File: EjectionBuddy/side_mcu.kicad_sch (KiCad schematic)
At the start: 2 parts, among them U6 STM32G031K8Ux

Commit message: Finished! QR and instruction pending
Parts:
- added C15: 10u, Capacitor_SMD:C_0603_1608Metric, symbol Device:C
- added C16, C17: 0.1u, Capacitor_SMD:C_0603_1608Metric, symbol Device:C
- added R21: 1k, Resistor_SMD:R_0603_1608Metric, symbol Device:R
- added SW1: SW_Push, Button_Switch_SMD:SW_SPST_PTS810, symbol Switch:SW_Push
- D11: footprint (none) -> Diode_SMD:D_SOD-523
- renumbered U6 to U7
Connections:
- net TX: now reaches U7.22 (PA9/PA11)
- net RX: now reaches U7.23 (PA10/PA12)
- net DIO: now reaches U7.24 (PA13)
- net CLK: now reaches U7.25 (PA14)
- net at U7.31 (PB7): now also D11.2 (A)
- net at U7.32 (PB8): now also R21.1
- net GND: now reaches U7.33 (VSS), U7.5 (VSS)
- net GND: now also C15.2, C16.2, C17.2, SW1.1
- net +3.3S: now reaches U7.4 (VDD)
- net +3.3S: now also C15.1, C16.1
- net RST: now reaches U7.6 (PF2)
- net RST: now also C17.1, SW1.2
- new net ONEWIRE: R21.2
- no-connect marks 0 -> 21
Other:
- note added: "PA14 is BOOT0"
- note added: "Protection from external pulling"
- note added: "Pull high to cut"
- moved on the sheet: U7

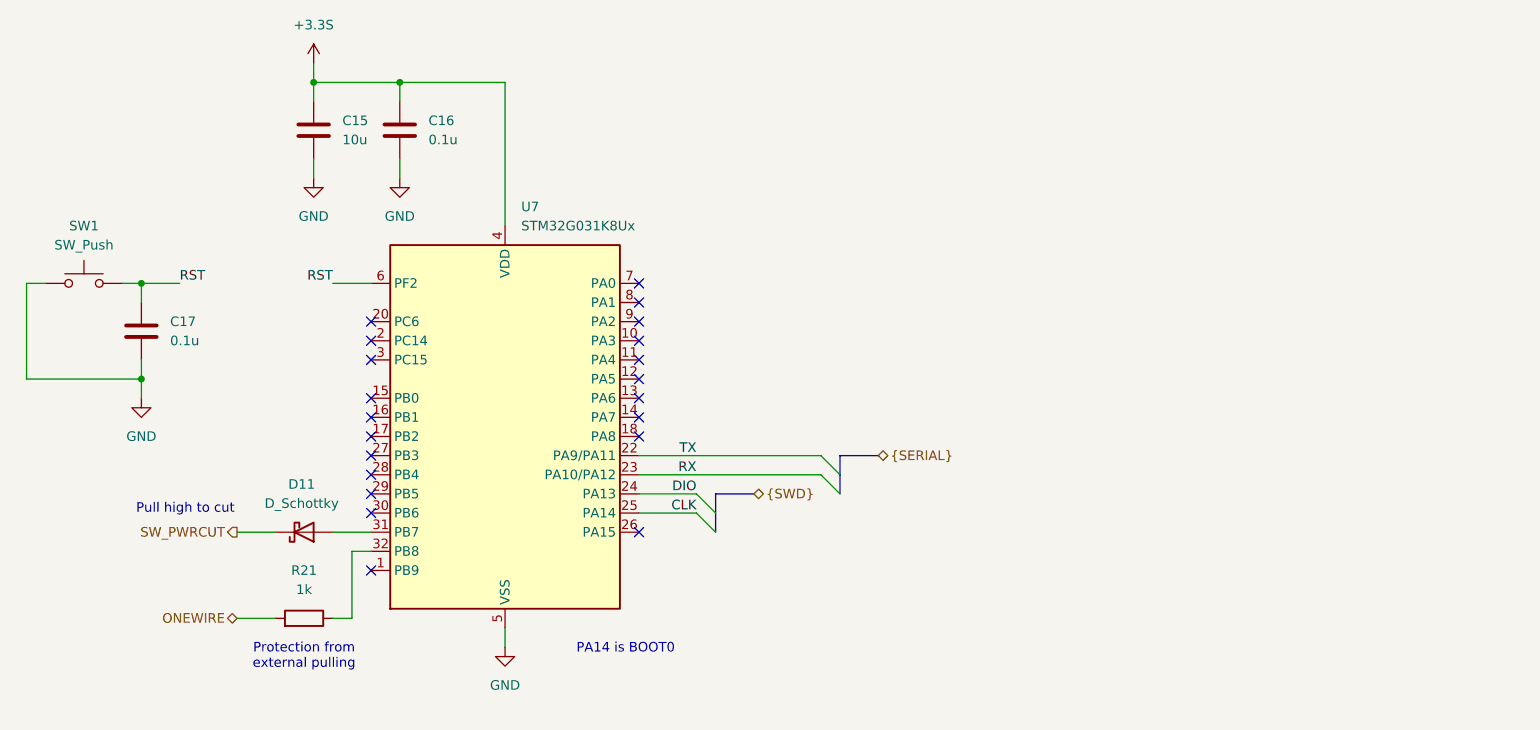
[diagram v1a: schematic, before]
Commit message: Slight improvements on routing and schematic
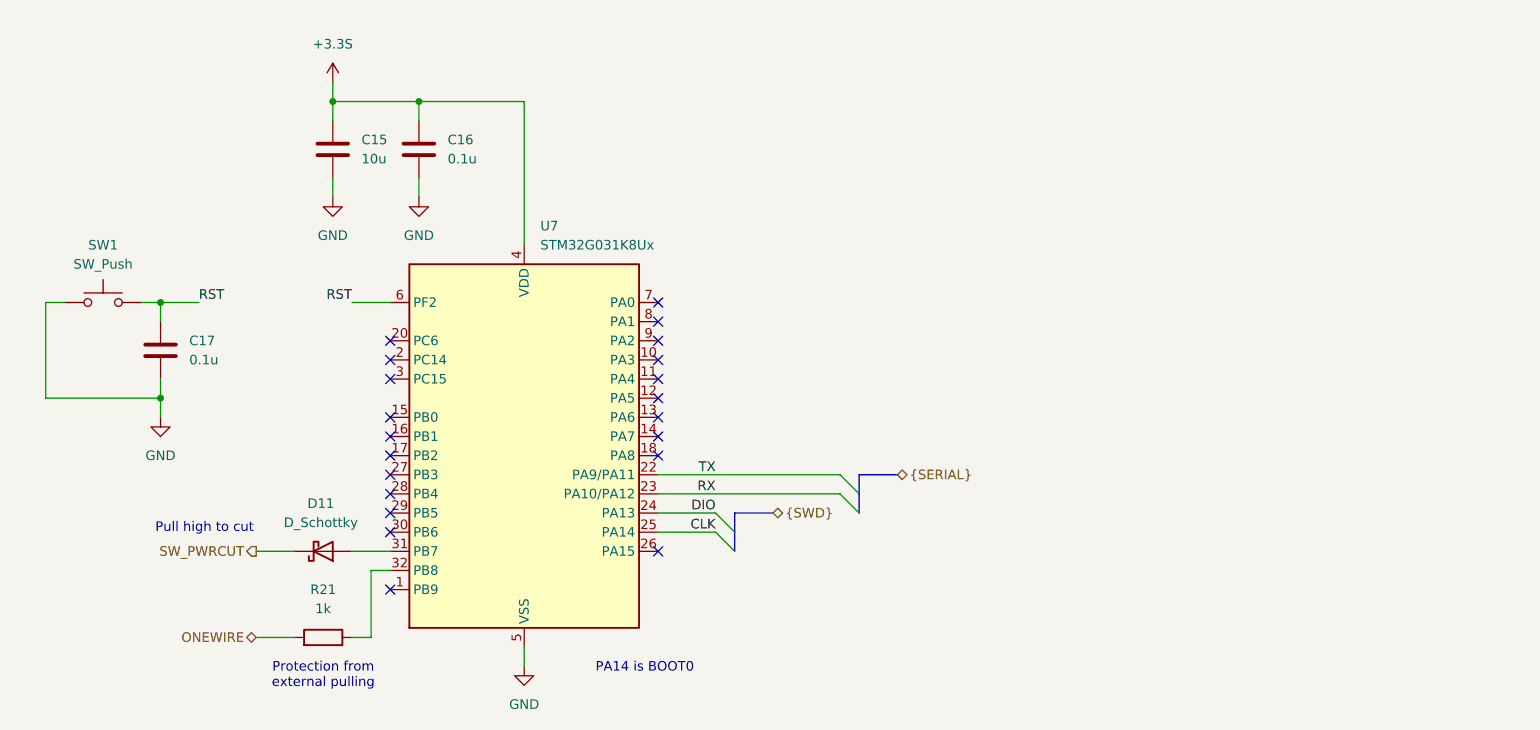
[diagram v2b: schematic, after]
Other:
- moved on the sheet: C15, C16, C17, D11, R21, SW1, U7

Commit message: Side-mcu stm -> attiny, with improvements here and there
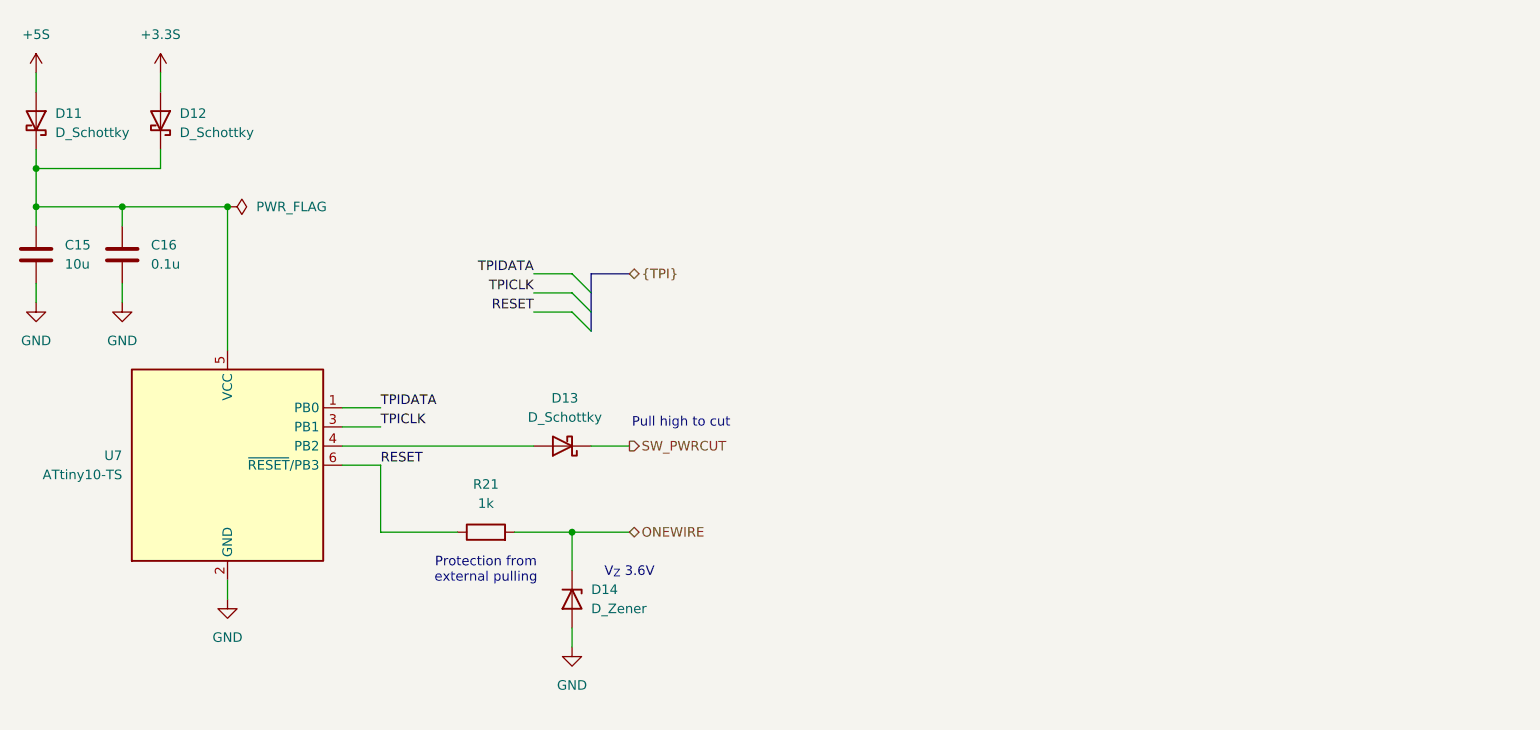
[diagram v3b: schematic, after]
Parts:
- removed C17: 0.1u, Capacitor_SMD:C_0603_1608Metric, symbol Device:C
- removed SW1: SW_Push, Button_Switch_SMD:SW_SPST_PTS810, symbol Switch:SW_Push
- removed U7: STM32G031K8Ux, Package_DFN_QFN:QFN-32-1EP_5x5mm_P0.5mm_EP3.45x3.45mm, symbol MCU_ST_STM32G0:STM32G031K8Ux
- added D12, D13: D_Schottky, Diode_SMD:D_SOD-523, symbol Device:D_Schottky
- added D14: D_Zener, Diode_SMD:D_SOD-523, symbol Device:D_Zener
- added U7: ATtiny10-TS, Package_TO_SOT_SMD:SOT-23-6, symbol MCU_Microchip_ATtiny:ATtiny10-TS
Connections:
- net +3.3S: now also D12.2 (A); no longer C15.1, C16.1
- net GND: now also D14.2 (A), U7.2 (GND)
- net ONEWIRE: now also D14.1 (K)
- net SW_PWRCUT: now also D13.1 (K); no longer D11.1 (K)
- net +5S: now reaches D11.2 (A)
- net RESET: now reaches R21.1
- net RESET: now also U7.6 (~{RESET}/PB3)
- new net: C15.1, C16.1, D11.1 (K), D12.1 (K), U7.5 (VCC)
- new net: D13.2 (A), U7.4 (PB2)
- new net TPICLK: U7.3 (PB1)
- new net TPIDATA: U7.1 (PB0)
- no-connect marks 21 -> 0
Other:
- note added: "V_{Z} 3.6V"
- note removed: "PA14 is BOOT0"

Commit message: Prodection version hw1.0 finished, with tidy-ups and bug-fixes
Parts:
- D14: value D_Zener -> D_Zener3V6
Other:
- moved on the sheet: C15, C16, D11, D12, D13, D14, R21, U7
